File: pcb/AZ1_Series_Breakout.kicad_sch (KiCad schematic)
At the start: 13 parts, among them J1 Conn_01x10, U1 NHD-C12832A1Z-FSRGB

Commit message: cleanup schema
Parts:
- C1, C2, C3, C4, C5, C6, C7, C8: Voltage (none) -> 16V
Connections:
- net VDD renamed +3V3
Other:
- company: (none) -> Perry Leumas
- title: (none) -> Newhaven Display AZ1 Breakout PCB
- moved on the sheet: C1, C2, C3, C4, C5, C6, C7, C8, J1, R1, R2, R3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

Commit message: add mounting holes
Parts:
- added H1, H2: MountingHole, MountingHole:MountingHole_3.2mm_M3_DIN965_Pad, symbol Mechanical:MountingHole
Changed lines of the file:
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@@
+	)
+	(symbol
+		(lib_id "Mechanical:MountingHole")
+		(at 102.87 127 0)
+		(unit 1)
+		(body_style 1)
+		(exclude_from_sim no)
+		(in_bom no)
+		(on_board yes)
+		(in_pos_files yes)
+		(dnp no)
+		(property "Reference" "H2"
+			(at 102.87 121.92 0)
+			(show_name no)
+			(do_not_autoplace no)
+			(effects
+				(font
+					(size 1.27 1.27)
+				)
+			)
+		)
+		(property "Value" "MountingHole"
+			(at 102.87 123.825 0)
+			(show_name no)
+			(do_not_autoplace no)
+			(effects
+				(font
+					(size 1.27 1.27)
+				)
+			)
+		)
+		(property "Footprint" "MountingHole:MountingHole_3.2mm_M3_DIN965_Pad"
+			(at 102.87 127 0)
+			(hide yes)
+			(show_name no)
+			(do_not_autoplace no)
+			(effects
+				(font
+					(size 1.27 1.27)
+				)
+			)
+		)
+		(property "Datasheet" ""
+			(at 102.87 127 0)
+			(hide yes)
+			(show_name no)
+			(do_not_autoplace no)
+			(effects
+				(font
+					(size 1.27 1.27)
+				)
+			)
+		)
+		(property "Description" "Mounting Hole without connection"
+			(at 102.87 127 0)
+			(hide yes)
+			(show_name no)
+			(do_not_autoplace no)
+			(effects
+				(font
+					(size 1.27 1.27)
+				)
+			)
+		)
+		(instances
+			(project "AZ1_Series_Breakout"
+				(path "/270788f4-b5d3-4481-9c95-b80269d19e59"
+					(reference "H2")
+					(unit 1)
+				)
+			)
+		)
 	)
 	(symbol
@@
 					(unit 1)
 				)
+			)
+		)
+	)
+	(symbol
+		(lib_id "Mechanical:MountingHole")
+		(at 88.9 127 0)
+		(unit 1)
+		(body_style 1)
+		(exclude_from_sim no)
+		(in_bom no)
+		(on_board yes)
+		(in_pos_files yes)
+		(dnp no)
+		(property "Reference" "H1"
+			(at 88.9 121.92 0)
+			(show_name no)
+			(do_not_autoplace no)
+			(effects
+				(font
+					(size 1.27 1.27)
+				)
+			)
+		)
+		(property "Value" "MountingHole"
+			(at 88.9 123.825 0)
+			(show_name no)
+			(do_not_autoplace no)
+			(effects
+				(font
+					(size 1.27 1.27)
+				)
+			)
+		)
+		(property "Footprint" "MountingHole:MountingHole_3.2mm_M3_DIN965_Pad"
+			(at 88.9 127 0)
+			(hide yes)
+			(show_name no)
+			(do_not_autoplace no)
+			(effects
+				(font
+					(size 1.27 1.27)
+				)
+			)
+		)
+		(property "Datasheet" ""
+			(at 88.9 127 0)
+			(hide yes)
+			(show_name no)
+			(do_not_autoplace no)
+			(effects
+				(font
+					(size 1.27 1.27)
+				)
+			)
+		)
+		(property "Description" "Mounting Hole without connection"
+			(at 88.9 127 0)
+			(hide yes)
+			(show_name no)
+			(do_not_autoplace no)
+			(effects
+				(font
+					(size 1.27 1.27)
+				)
+			)
+		)
+		(instances
+			(project "AZ1_Series_Breakout"
+				(path "/270788f4-b5d3-4481-9c95-b80269d19e59"
+					(reference "H1")
+					(unit 1)
+				)

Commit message: swap RST and CS1B for easy layout
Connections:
- net ~{CS1B}: now also J1.6 (Pin_6); no longer J1.5 (Pin_5)
- net ~{RST}: now also J1.5 (Pin_5); no longer J1.6 (Pin_6)
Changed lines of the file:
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@@
 	)
 	(label "~{RST}"
-		(at 80.01 92.71 0)
+		(at 80.01 90.17 0)
 		(effects
 			(font
@@
 	)
 	(label "~{CS1B}"
-		(at 80.01 90.17 0)
+		(at 80.01 92.71 0)
 		(effects
 			(font

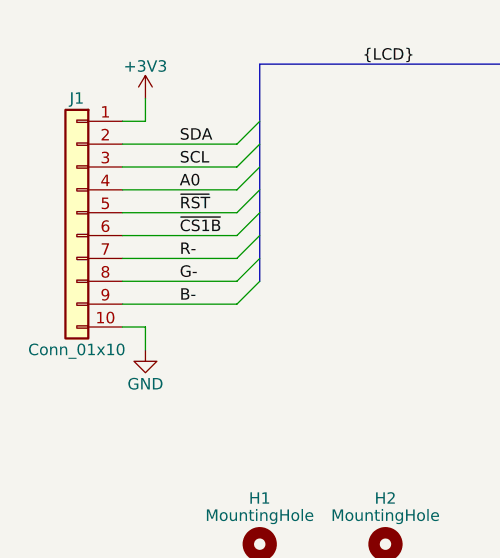
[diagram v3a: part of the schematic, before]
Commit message: shift header pinout
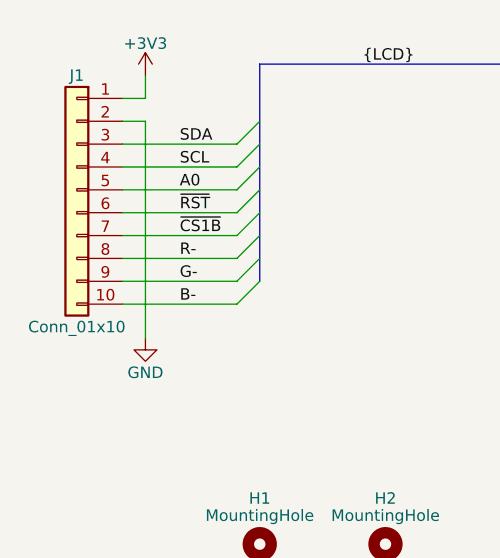
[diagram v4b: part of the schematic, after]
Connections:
- net A0: now also J1.5 (Pin_5); no longer J1.4 (Pin_4)
- net B-: now also J1.10 (Pin_10); no longer J1.9 (Pin_9)
- net G-: now also J1.9 (Pin_9); no longer J1.8 (Pin_8)
- net GND: now also J1.2 (Pin_2); no longer J1.10 (Pin_10)
- net R-: now also J1.8 (Pin_8); no longer J1.7 (Pin_7)
- net SCL: now also J1.4 (Pin_4); no longer J1.3 (Pin_3)
- net SDA: now also J1.3 (Pin_3); no longer J1.2 (Pin_2)
- net ~{CS1B}: now also J1.7 (Pin_7); no longer J1.6 (Pin_6)
- net ~{RST}: now also J1.6 (Pin_6); no longer J1.5 (Pin_5)
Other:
- moved on the sheet: J1
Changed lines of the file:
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@@
+	(wire
+		(pts
+			(xy 76.2 80.01) (xy 76.2 104.14)
+		)
+		(stroke
+			(width 0)
+			(type default)
+		)
+	)
 	(wire
 		(pts
@@
 	(wire
 		(pts
-			(xy 76.2 105.41) (xy 76.2 102.87)
-		)
-		(stroke
-			(width 0)
-			(type default)
-		)
-	)
-	(wire
-		(pts
 			(xy 73.66 97.79) (xy 86.36 97.79)
 		)
@@
 		)
 	)
-	(wire
-		(pts
-			(xy 76.2 102.87) (xy 73.66 102.87)
-		)
-		(stroke
-			(width 0)
-			(type default)
-		)
-	)
 	(bus
 		(pts
@@
 	(wire
 		(pts
-			(xy 76.2 80.01) (xy 76.2 77.47)
+			(xy 76.2 77.47) (xy 76.2 74.93)
 		)
 		(stroke
@@
 	(wire
 		(pts
+			(xy 73.66 80.01) (xy 76.2 80.01)
+		)
+		(stroke
+			(width 0)
+			(type default)
+		)
+	)
+	(wire
+		(pts
 			(xy 194.31 106.68) (xy 172.72 106.68)
 		)
@@
 	(wire
 		(pts
-			(xy 73.66 80.01) (xy 76.2 80.01)
+			(xy 73.66 77.47) (xy 76.2 77.47)
 		)
 		(stroke
@@
 	(symbol
 		(lib_id "power:GND")
-		(at 76.2 105.41 0)
+		(at 76.2 104.14 0)
 		(unit 1)
 		(body_style 1)
@@
 		(dnp no)
 		(property "Reference" "#PWR011"
-			(at 76.2 111.76 0)
+			(at 76.2 110.49 0)
 			(hide yes)
 			(show_name no)
@@
 		)
 		(property "Value" "GND"
-			(at 76.2 109.22 0)
+			(at 76.2 107.95 0)
 			(show_name no)
 			(do_not_autoplace no)
@@
 		)
 		(property "Footprint" "Display:NHD-C12832A1Z-FSRGB"
-			(at 76.2 105.41 0)
+			(at 76.2 104.14 0)
 			(hide yes)
 			(show_name no)
@@
 		)
 		(property "Datasheet" ""
-			(at 76.2 105.41 0)
+			(at 76.2 104.14 0)
 			(hide yes)
 			(show_name no)
@@
 		)
 		(property "Description" "Power symbol creates a global label with name \"GND\" , ground"
-			(at 76.2 105.41 0)
+			(at 76.2 104.14 0)
 			(hide yes)
 			(show_name no)
@@
 	(symbol
 		(lib_id "Connector_Generic:Conn_01x10")
-		(at 68.58 90.17 0)
+		(at 68.58 87.63 0)
 		(mirror y)
 		(unit 1)
@@
 		(dnp no)
 		(property "Reference" "J1"
-			(at 68.58 77.47 0)
+			(at 68.58 74.93 0)
 			(show_name no)
 			(do_not_autoplace no)
@@
 		)
 		(property "Value" "Conn_01x10"
-			(at 68.58 105.41 0)
+			(at 68.58 102.87 0)
 			(show_name no)
 			(do_not_autoplace no)
@@
 		)
 		(property "Footprint" "Connector_PinHeader_2.54mm:PinHeader_1x10_P2.54mm_Vertical"
-			(at 68.58 90.17 0)
+			(at 68.58 87.63 0)
 			(hide yes)
 			(show_name no)
@@
 		)
 		(property "Datasheet" ""
-			(at 68.58 90.17 0)
+			(at 68.58 87.63 0)
 			(hide yes)
 			(show_name no)
@@
 		)
 		(property "Description" "Generic connector, single row, 01x10, script generated (kicad-library-utils/schlib/autogen/connector/)"
-			(at 68.58 90.17 0)
+			(at 68.58 87.63 0)
 			(hide yes)
 			(show_name no)
@@
 		)
 		(property "Voltage" ""
-			(at 68.58 90.17 0)
+			(at 68.58 87.63 0)
 			(hide yes)
 			(show_name no)
@@
 	(symbol
 		(lib_id "power:+3V3")
-		(at 76.2 77.47 0)
+		(at 76.2 74.93 0)
 		(unit 1)
 		(body_style 1)
@@
 		(dnp no)
 		(property "Reference" "#PWR012"
-			(at 76.2 81.28 0)
+			(at 76.2 78.74 0)
 			(hide yes)
 			(show_name no)
@@
 		)
 		(property "Value" "+3V3"
-			(at 76.2 73.914 0)
+			(at 76.2 71.374 0)
 			(show_name no)
 			(do_not_autoplace no)
@@
 		)
 		(property "Footprint" ""
-			(at 76.2 77.47 0)
+			(at 76.2 74.93 0)
 			(hide yes)
 			(show_name no)
@@
 		)
 		(property "Datasheet" ""
-			(at 76.2 77.47 0)
+			(at 76.2 74.93 0)
 			(hide yes)
 			(show_name no)
@@
 		)
 		(property "Description" "Power symbol creates a global label with name \"+3V3\""
-			(at 76.2 77.47 0)
-			(hide yes)
-			(show_name no)
+			(at 76.2 74.93 0)
+			(hide yes)
+			(show_name no)
